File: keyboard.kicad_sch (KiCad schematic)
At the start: 33 parts, among them IC2 80C51, IC3 74LS145, IC4 74LS145, IC7 74LS366, IC9 74LS241

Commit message: prepare for fabrication
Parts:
- C76, C77, C87: LCSC (none) -> C344201; LCSC Part (none) -> C344201
- IC3, IC4: LCSC (none) -> C60829; LCSC Part (none) -> C60829
- IC9: LCSC (none) -> C2676097; LCSC Part (none) -> C2676097
- R49: LCSC (none) -> C2907326; LCSC Part (none) -> C2907326
- R64, R79: LCSC (none) -> C2907219; LCSC Part (none) -> C2907219
- R71, R72: LCSC (none) -> C17630; LCSC Part (none) -> C17630
- R77: LCSC (none) -> C17557; LCSC Part (none) -> C17557
- R78, R80: LCSC (none) -> C17590; LCSC Part (none) -> C17590
- RP3: LCSC (none) -> C1739866; LCSC Part (none) -> C1739866
- TP12, TP13, TP14: now not fitted

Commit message: verify all component values vs TRM
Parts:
- C86: value 47uF -> 47uF 16V
- FS5: value 0A25 -> 250MA 63VAC
- IC2: value 80C51 -> Intel 80C51
- R49: value 4K7 -> 4K7 5% 0.1W
- R64, R79: value 10K -> 10K 5% 0.1W
- R71, R72: value 330R -> 330R 5% 0.1W
- R77: value 220R -> 220R 5% 0.1W
- R78, R80: value 270R -> 270R 5% 0.1W
- RP3: value 47K -> 47Kx15 5%
- SK2, SK3: value 20WAYFLEX -> 0801,202 20 way flex
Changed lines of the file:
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@@
 			)
 		)
-		(property "Value" "4K7"
+		(property "Value" "4K7 5% 0.1W"
 			(at 57.658 184.912 90)
 			(effects
@@
 			)
 		)
-		(property "Value" "47K"
+		(property "Value" "47Kx15 5%"
 			(at 203.2 313.69 0)
 			(effects
@@
 			)
 		)
-		(property "Value" "330R"
+		(property "Value" "330R 5% 0.1W"
 			(at 84.328 276.352 90)
 			(effects
@@
 			)
 		)
-		(property "Value" "47K"
+		(property "Value" "47Kx15 5%"
 			(at 191.77 313.69 0)
 			(effects
@@
 			)
 		)
-		(property "Value" "47K"
+		(property "Value" "47Kx15 5%"
 			(at 160.02 313.69 0)
 			(effects
@@
 			)
 		)
-		(property "Value" "47K"
+		(property "Value" "47Kx15 5%"
 			(at 170.18 313.69 0)
 			(effects
@@
 			)
 		)
-		(property "Value" "270R"
+		(property "Value" "270R 5% 0.1W"
 			(at 154.178 253.492 90)
 			(effects
@@
 			)
 		)
-		(property "Value" "47K"
+		(property "Value" "47Kx15 5%"
 			(at 148.59 313.69 0)
 			(effects
@@
 			)
 		)
-		(property "Value" "47K"
+		(property "Value" "47Kx15 5%"
 			(at 110.49 171.45 0)
 			(effects
@@
 			)
 		)
-		(property "Value" "47K"
+		(property "Value" "47Kx15 5%"
 			(at 114.3 171.45 0)
 			(effects
@@
 			)
 		)
-		(property "Value" "47K"
+		(property "Value" "47Kx15 5%"
 			(at 118.11 171.45 0)
 			(effects
@@
 			)
 		)
-		(property "Value" "10K"
+		(property "Value" "10K 5% 0.1W"
 			(at 113.538 243.332 90)
 			(effects
@@
 			)
 		)
-		(property "Value" "47K"
+		(property "Value" "47Kx15 5%"
 			(at 121.92 171.45 0)
 			(effects
@@
 			)
 		)
-		(property "Value" "47K"
+		(property "Value" "47Kx15 5%"
 			(at 99.06 171.45 0)
 			(effects
@@
 			)
 		)
-		(property "Value" "330R"
+		(property "Value" "330R 5% 0.1W"
 			(at 84.328 267.462 90)
 			(effects
@@
 			)
 		)
-		(property "Value" "0A25"
+		(property "Value" "250MA 63VAC"
 			(at 34.29 66.04 90)
 			(effects
@@
 			)
 		)
-		(property "Value" "47K"
+		(property "Value" "47Kx15 5%"
 			(at 180.34 313.69 0)
 			(effects
@@
 			)
 		)
-		(property "Value" "47K"
+		(property "Value" "47Kx15 5%"
 			(at 213.36 313.69 0)
 			(effects
@@
 			)
 		)
-		(property "Value" "47K"
+		(property "Value" "47Kx15 5%"
 			(at 106.68 171.45 0)
 			(effects
@@
 			)
 		)
-		(property "Value" "20WAYFLEX"
+		(property "Value" "0801,202 20 way flex"
 			(at 245.11 129.54 90)
 			(effects
@@
 			)
 		)
-		(property "Value" "270R"
+		(property "Value" "270R 5% 0.1W"
 			(at 154.178 248.412 90)
 			(effects
@@
 			)
 		)
-		(property "Value" "20WAYFLEX"
+		(property "Value" "0801,202 20 way flex"
 			(at 245.11 182.88 90)
 			(effects
@@
 			)
 		)
-		(property "Value" "220R"
+		(property "Value" "220R 5% 0.1W"
 			(at 154.178 256.032 90)
 			(effects
@@
 			)
 		)
-		(property "Value" "47K"
+		(property "Value" "47Kx15 5%"
 			(at 125.73 171.45 0)
 			(effects
@@
 			)
 		)
-		(property "Value" "10K"
+		(property "Value" "10K 5% 0.1W"
 			(at 113.538 250.952 90)
 			(effects
@@
 			)
 		)
-		(property "Value" "47uF"
+		(property "Value" "47uF 16V"
 			(at 108.458 76.2 0)
 			(effects
@@
 			)
 		)
-		(property "Value" "47K"
+		(property "Value" "47Kx15 5%"
 			(at 102.87 171.45 0)
 			(effects
@@
 			)
 		)
-		(property "Value" "80C51"
+		(property "Value" "Intel 80C51"
 			(at 80.9341 139.7 0)
 			(effects

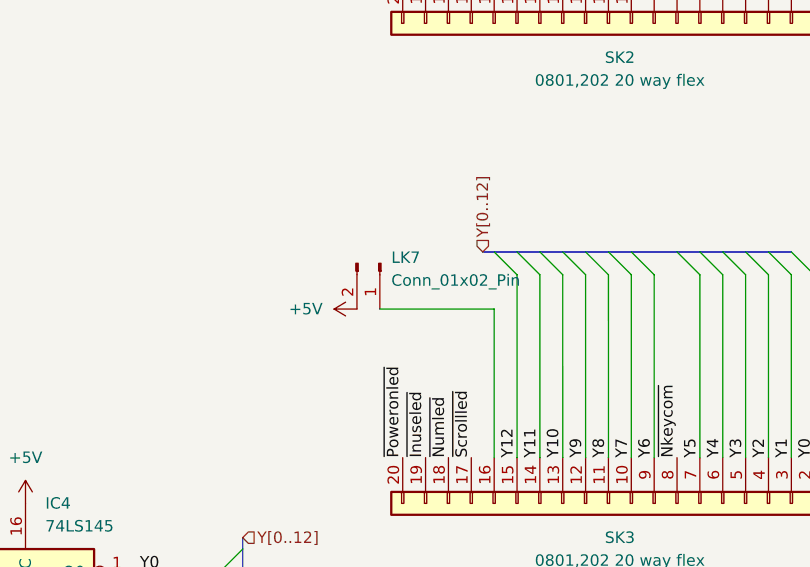
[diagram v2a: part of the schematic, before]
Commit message: fix power domain links with net ties
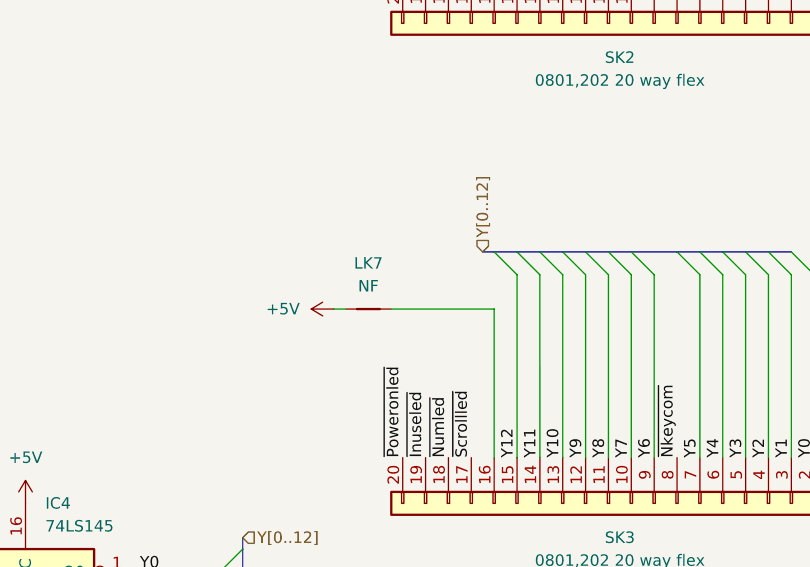
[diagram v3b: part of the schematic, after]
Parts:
- removed LK7: Conn_01x02_Pin, Connector_PinHeader_2.54mm:PinHeader_1x02_P2.54mm_Vertical, symbol Connector:Conn_01x02_Pin
- added LK7: NF, Acorn:Link_Connected, symbol Device:NetTie_2
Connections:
- net +5V: now also LK7.1
- net at SK3.16 (Pin_16): now also LK7.2
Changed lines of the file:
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@@
 		)
 	)
+	(wire
+		(pts
+			(xy 213.36 154.94) (xy 214.63 154.94)
+		)
+		(stroke
+			(width 0)
+			(type default)
+		)
+	)
 	(bus
 		(pts
@@
 	(wire
 		(pts
-			(xy 218.44 154.94) (xy 231.14 154.94)
+			(xy 219.71 154.94) (xy 231.14 154.94)
 		)
 		(stroke
@@
 	)
 	(symbol
+		(lib_id "Device:NetTie_2")
+		(at 217.17 154.94 0)
+		(unit 1)
+		(exclude_from_sim no)
+		(in_bom no)
+		(on_board yes)
+		(dnp no)
+		(fields_autoplaced yes)
+		(property "Reference" "LK7"
+			(at 217.17 149.86 0)
+			(effects
+				(font
+					(size 1.27 1.27)
+				)
+			)
+		)
+		(property "Value" "NF"
+			(at 217.17 152.4 0)
+			(effects
+				(font
+					(size 1.27 1.27)
+				)
+			)
+		)
+		(property "Footprint" "Acorn:Link_Connected"
+			(at 217.17 154.94 0)
+			(effects
+				(font
+					(size 1.27 1.27)
+				)
+				(hide yes)
+			)
+		)
+		(property "Datasheet" "~"
+			(at 217.17 154.94 0)
+			(effects
+				(font
+					(size 1.27 1.27)
+				)
+				(hide yes)
+			)
+		)
+		(property "Description" "Net tie, 2 pins"
+			(at 217.17 154.94 0)
+			(effects
+				(font
+					(size 1.27 1.27)
+				)
+				(hide yes)
+			)
+		)
+		(pin "2"
+		)
+		(pin "1"
+		)
+		(instances
+			(project "Acorn-A3010"
+				(path "/999882f3-94f8-4a89-9093-27a47d0cb289/20613dd3-c886-4190-96bd-e62e2e571bea"
+					(reference "LK7")
+					(unit 1)
+				)
+			)
+		)
+	)
+	(symbol
 		(lib_id "power:GND")
 		(at 120.65 232.41 0)
@@
 	)
 	(symbol
-		(lib_id "Connector:Conn_01x02_Pin")
-		(at 218.44 149.86 270)
-		(unit 1)
-		(exclude_from_sim no)
-		(in_bom yes)
-		(on_board yes)
-		(dnp no)
-		(fields_autoplaced yes)
-		(property "Reference" "LK7"
-			(at 219.71 149.2249 90)
-			(effects
-				(font
-					(size 1.27 1.27)
-				)
-				(justify left)
-			)
-		)
-		(property "Value" "Conn_01x02_Pin"
-			(at 219.71 151.7649 90)
-			(effects
-				(font
-					(size 1.27 1.27)
-				)
-				(justify left)
-			)
-		)
-		(property "Footprint" "Connector_PinHeader_2.54mm:PinHeader_1x02_P2.54mm_Vertical"
-			(at 218.44 149.86 0)
-			(effects
-				(font
-					(size 1.27 1.27)
-				)
-				(hide yes)
-			)
-		)
-		(property "Datasheet" "~"
-			(at 218.44 149.86 0)
-			(effects
-				(font
-					(size 1.27 1.27)
-				)
-				(hide yes)
-			)
-		)
-		(property "Description" "Generic connector, single row, 01x02, script generated"
-			(at 218.44 149.86 0)
-			(effects
-				(font
-					(size 1.27 1.27)
-				)
-				(hide yes)
-			)
-		)
-		(pin "2"
-		)
-		(pin "1"
-		)
-		(instances
-			(project "Acorn-A3010"
-				(path "/999882f3-94f8-4a89-9093-27a47d0cb289/20613dd3-c886-4190-96bd-e62e2e571bea"
-					(reference "LK7")
-					(unit 1)
-				)
-			)
-		)
-	)
-	(symbol
 		(lib_id "power:GND")
 		(at 101.6 120.65 0)
@@
 	(symbol
 		(lib_id "power:+5V")
-		(at 215.9 154.94 90)
+		(at 213.36 154.94 90)
 		(unit 1)
 		(exclude_from_sim no)
@@
 		(fields_autoplaced yes)
 		(property "Reference" "#PWR0171"
-			(at 219.71 154.94 0)
+			(at 217.17 154.94 0)
 			(effects
 				(font
@@
 		)
 		(property "Value" "+5V"
-			(at 212.09 154.9399 90)
+			(at 209.55 154.9399 90)
 			(effects
 				(font
@@
 		)
 		(property "Footprint" ""
-			(at 215.9 154.94 0)
+			(at 213.36 154.94 0)
 			(effects
 				(font
@@
 		)
 		(property "Datasheet" ""
-			(at 215.9 154.94 0)
+			(at 213.36 154.94 0)
 			(effects
 				(font
@@
 		)
 		(property "Description" "Power symbol creates a global label with name \"+5V\""
-			(at 215.9 154.94 0)
+			(at 213.36 154.94 0)
 			(effects
 				(font
